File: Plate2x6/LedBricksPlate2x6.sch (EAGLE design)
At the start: 8 parts

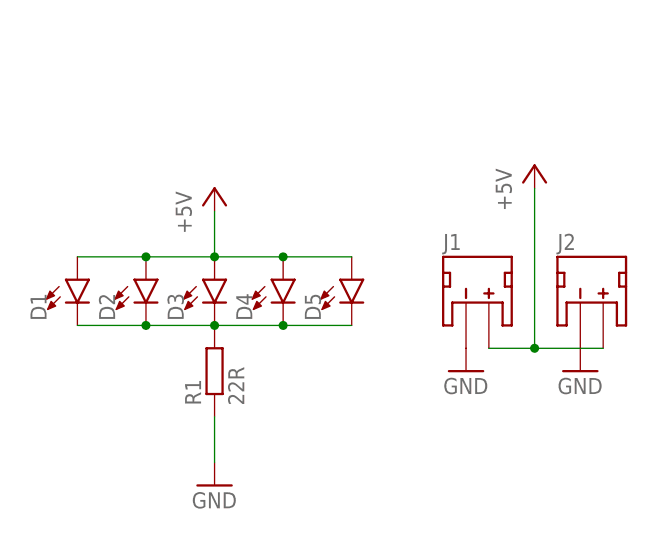
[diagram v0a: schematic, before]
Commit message: change connector to jst sh
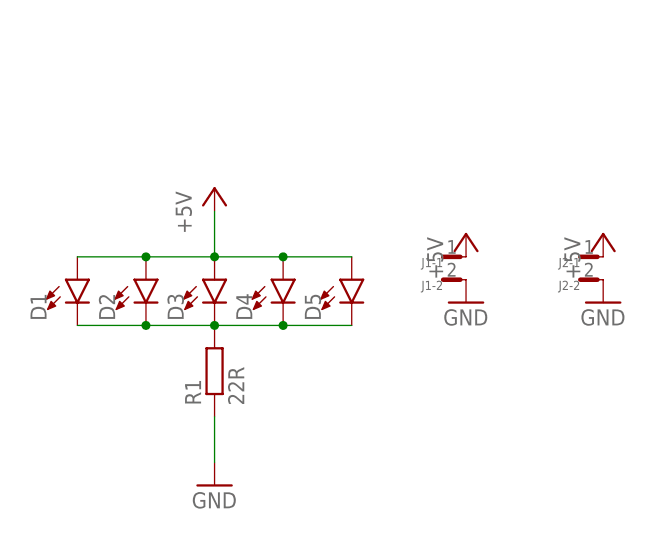
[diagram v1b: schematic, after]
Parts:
- J1, J2: value (none) -> SM02B-SRSS-TB; device SparkFun-Connectors:JST_2MM_MALE -> con-JST-SH:SM02B-SRSS-TB
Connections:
- net +5V: now also J1-1.P, J2-1.P; no longer J1.+, J2.+
- net GND: now also J1-2.P, J2-2.P; no longer J1.-, J2.-
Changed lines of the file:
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@@
 <part name="P+1" library="supply1" library_urn="urn:adsk.eagle:library:371" deviceset="+5V" device=""/>
 <part name="GND1" library="supply1" library_urn="urn:adsk.eagle:library:371" deviceset="GND" device=""/>
-<part name="J1" library="SparkFun-Connectors" library_urn="urn:adsk.eagle:library:513" deviceset="JST_2MM_MALE" device="" package3d_urn="urn:adsk.eagle:package:38042/1"/>
-<part name="J2" library="SparkFun-Connectors" library_urn="urn:adsk.eagle:library:513" deviceset="JST_2MM_MALE" device="" package3d_urn="urn:adsk.eagle:package:38042/1"/>
 <part name="GND2" library="supply1" library_urn="urn:adsk.eagle:library:371" deviceset="GND" device=""/>
 <part name="GND3" library="supply1" library_urn="urn:adsk.eagle:library:371" deviceset="GND" device=""/>
 <part name="P+2" library="supply1" library_urn="urn:adsk.eagle:library:371" deviceset="+5V" device=""/>
+<part name="J1" library="con-JST-SH" deviceset="SM02B-SRSS-TB" device=""/>
+<part name="J2" library="con-JST-SH" deviceset="SM02B-SRSS-TB" device=""/>
+<part name="P+3" library="supply1" library_urn="urn:adsk.eagle:library:371" deviceset="+5V" device=""/>
 </parts>
 <sheets>
@@
 <attribute name="VALUE" x="15.24" y="-25.4" size="1.778" layer="96"/>
 </instance>
-<instance part="J1" gate="G$1" x="45.72" y="-2.54" smashed="yes">
-<attribute name="NAME" x="43.18" y="3.302" size="1.778" layer="95"/>
+<instance part="GND2" gate="1" x="45.72" y="-2.54" smashed="yes">
+<attribute name="VALUE" x="43.18" y="-5.08" size="1.778" layer="96"/>
 </instance>
-<instance part="J2" gate="G$1" x="58.42" y="-2.54" smashed="yes">
-<attribute name="NAME" x="55.88" y="3.302" size="1.778" layer="95"/>
+<instance part="GND3" gate="1" x="60.96" y="-2.54" smashed="yes">
+<attribute name="VALUE" x="58.42" y="-5.08" size="1.778" layer="96"/>
 </instance>
-<instance part="GND2" gate="1" x="45.72" y="-10.16" smashed="yes">
-<attribute name="VALUE" x="43.18" y="-12.7" size="1.778" layer="96"/>
+<instance part="P+2" gate="1" x="45.72" y="5.08" smashed="yes">
+<attribute name="VALUE" x="43.18" y="0" size="1.778" layer="96" rot="R90"/>
 </instance>
-<instance part="GND3" gate="1" x="58.42" y="-10.16" smashed="yes">
-<attribute name="VALUE" x="55.88" y="-12.7" size="1.778" layer="96"/>
+<instance part="J1" gate="-1" x="43.18" y="2.54" smashed="yes">
+<attribute name="NAME" x="43.18" y="1.905" size="1.016" layer="95" rot="R180" align="center-left"/>
 </instance>
-<instance part="P+2" gate="1" x="53.34" y="12.7" smashed="yes">
-<attribute name="VALUE" x="50.8" y="7.62" size="1.778" layer="96" rot="R90"/>
+<instance part="J1" gate="-2" x="43.18" y="0" smashed="yes">
+<attribute name="NAME" x="43.18" y="-0.635" size="1.016" layer="95" rot="R180" align="center-left"/>
+</instance>
+<instance part="J2" gate="-1" x="58.42" y="2.54" smashed="yes">
+<attribute name="NAME" x="58.42" y="1.905" size="1.016" layer="95" rot="R180" align="center-left"/>
+</instance>
+<instance part="J2" gate="-2" x="58.42" y="0" smashed="yes">
+<attribute name="NAME" x="58.42" y="-0.635" size="1.016" layer="95" rot="R180" align="center-left"/>
+</instance>
+<instance part="P+3" gate="1" x="60.96" y="5.08" smashed="yes">
+<attribute name="VALUE" x="58.42" y="0" size="1.778" layer="96" rot="R90"/>
 </instance>
 </instances>
@@
 </segment>
 <segment>
-<pinref part="J1" gate="G$1" pin="+"/>
-<pinref part="J2" gate="G$1" pin="+"/>
-<wire x1="48.26" y1="-7.62" x2="53.34" y2="-7.62" width="0.1524" layer="91"/>
-<wire x1="53.34" y1="-7.62" x2="60.96" y2="-7.62" width="0.1524" layer="91"/>
-<wire x1="53.34" y1="-7.62" x2="53.34" y2="10.16" width="0.1524" layer="91"/>
-<junction x="53.34" y="-7.62"/>
+<pinref part="J1" gate="-1" pin="P"/>
 <pinref part="P+2" gate="1" pin="+5V"/>
+</segment>
+<segment>
+<pinref part="J2" gate="-1" pin="P"/>
+<pinref part="P+3" gate="1" pin="+5V"/>
 </segment>
 </net>
@@
 </segment>
 <segment>
-<pinref part="J1" gate="G$1" pin="-"/>
+<pinref part="J1" gate="-2" pin="P"/>
 <pinref part="GND2" gate="1" pin="GND"/>
 </segment>
 <segment>
-<pinref part="J2" gate="G$1" pin="-"/>
+<pinref part="J2" gate="-2" pin="P"/>
 <pinref part="GND3" gate="1" pin="GND"/>
 </segment>

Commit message: gerbers, pnp file
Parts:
- D1, D2, D3, D4, D5: value (none) -> XL-3216WWC
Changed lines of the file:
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@@
 </classes>
 <parts>
-<part name="D1" library="SparkFun-LED" library_urn="urn:adsk.eagle:library:529" deviceset="LED" device="1206" package3d_urn="urn:adsk.eagle:package:39352/1"/>
-<part name="D2" library="SparkFun-LED" library_urn="urn:adsk.eagle:library:529" deviceset="LED" device="1206" package3d_urn="urn:adsk.eagle:package:39352/1"/>
-<part name="D3" library="SparkFun-LED" library_urn="urn:adsk.eagle:library:529" deviceset="LED" device="1206" package3d_urn="urn:adsk.eagle:package:39352/1"/>
-<part name="D4" library="SparkFun-LED" library_urn="urn:adsk.eagle:library:529" deviceset="LED" device="1206" package3d_urn="urn:adsk.eagle:package:39352/1"/>
-<part name="D5" library="SparkFun-LED" library_urn="urn:adsk.eagle:library:529" deviceset="LED" device="1206" package3d_urn="urn:adsk.eagle:package:39352/1"/>
+<part name="D1" library="SparkFun-LED" library_urn="urn:adsk.eagle:library:529" deviceset="LED" device="1206" package3d_urn="urn:adsk.eagle:package:39352/1" value="XL-3216WWC"/>
+<part name="D2" library="SparkFun-LED" library_urn="urn:adsk.eagle:library:529" deviceset="LED" device="1206" package3d_urn="urn:adsk.eagle:package:39352/1" value="XL-3216WWC"/>
+<part name="D3" library="SparkFun-LED" library_urn="urn:adsk.eagle:library:529" deviceset="LED" device="1206" package3d_urn="urn:adsk.eagle:package:39352/1" value="XL-3216WWC"/>
+<part name="D4" library="SparkFun-LED" library_urn="urn:adsk.eagle:library:529" deviceset="LED" device="1206" package3d_urn="urn:adsk.eagle:package:39352/1" value="XL-3216WWC"/>
+<part name="D5" library="SparkFun-LED" library_urn="urn:adsk.eagle:library:529" deviceset="LED" device="1206" package3d_urn="urn:adsk.eagle:package:39352/1" value="XL-3216WWC"/>
 <part name="R1" library="resistor" library_urn="urn:adsk.eagle:library:348" deviceset="R-EU_" device="R0805" package3d_urn="urn:adsk.eagle:package:23553/2" value="22R"/>
 <part name="P+1" library="supply1" library_urn="urn:adsk.eagle:library:371" deviceset="+5V" device=""/>
@@
 <instances>
 <instance part="D1" gate="G$1" x="2.54" y="0" smashed="yes">
-<attribute name="NAME" x="-0.889" y="-4.572" size="1.778" layer="95" font="vector" rot="R90"/>
-<attribute name="VALUE" x="4.445" y="-4.572" size="1.778" layer="96" font="vector" rot="R90" align="top-left"/>
+<attribute name="NAME" x="3.556" y="-4.699" size="1.778" layer="95" font="vector"/>
+<attribute name="VALUE" x="-3.175" y="0.508" size="1.778" layer="96" font="vector" rot="R90" align="top-left"/>
 </instance>
 <instance part="D2" gate="G$1" x="10.16" y="0" smashed="yes">
-<attribute name="NAME" x="6.731" y="-4.572" size="1.778" layer="95" font="vector" rot="R90"/>
-<attribute name="VALUE" x="12.065" y="-4.572" size="1.778" layer="96" font="vector" rot="R90" align="top-left"/>
+<attribute name="NAME" x="11.176" y="-4.445" size="1.778" layer="95" font="vector"/>
+<attribute name="VALUE" x="4.445" y="0.508" size="1.778" layer="96" font="vector" rot="R90" align="top-left"/>
 </instance>
 <instance part="D3" gate="G$1" x="17.78" y="0" smashed="yes">
-<attribute name="NAME" x="14.351" y="-4.572" size="1.778" layer="95" font="vector" rot="R90"/>
-<attribute name="VALUE" x="19.685" y="-4.572" size="1.778" layer="96" font="vector" rot="R90" align="top-left"/>
+<attribute name="NAME" x="18.796" y="-4.445" size="1.778" layer="95" font="vector"/>
+<attribute name="VALUE" x="14.605" y="0.508" size="1.778" layer="96" font="vector" rot="R90" align="top-left"/>
 </instance>
 <instance part="D4" gate="G$1" x="25.4" y="0" smashed="yes">
-<attribute name="NAME" x="21.971" y="-4.572" size="1.778" layer="95" font="vector" rot="R90"/>
-<attribute name="VALUE" x="27.305" y="-4.572" size="1.778" layer="96" font="vector" rot="R90" align="top-left"/>
+<attribute name="NAME" x="26.67" y="-4.445" size="1.778" layer="95" font="vector"/>
+<attribute name="VALUE" x="24.511" y="3.81" size="1.778" layer="96" font="vector" rot="R90" align="top-left"/>
 </instance>
 <instance part="D5" gate="G$1" x="33.02" y="0" smashed="yes">
-<attribute name="NAME" x="29.591" y="-4.572" size="1.778" layer="95" font="vector" rot="R90"/>
-<attribute name="VALUE" x="34.925" y="-4.572" size="1.778" layer="96" font="vector" rot="R90" align="top-left"/>
+<attribute name="NAME" x="34.798" y="-5.715" size="1.778" layer="95" font="vector"/>
+<attribute name="VALUE" x="32.131" y="3.048" size="1.778" layer="96" font="vector" rot="R90" align="top-left"/>
 </instance>
 <instance part="R1" gate="G$1" x="17.78" y="-10.16" smashed="yes" rot="R90">
-<attribute name="NAME" x="16.2814" y="-13.97" size="1.778" layer="95" rot="R90"/>
-<attribute name="VALUE" x="21.082" y="-13.97" size="1.778" layer="96" rot="R90"/>
+<attribute name="NAME" x="20.066" y="-11.4554" size="1.778" layer="95"/>
+<attribute name="VALUE" x="20.066" y="-14.224" size="1.778" layer="96"/>
 </instance>
-<instance part="P+1" gate="1" x="17.78" y="10.16" smashed="yes">
-<attribute name="VALUE" x="15.24" y="5.08" size="1.778" layer="96" rot="R90"/>
+<instance part="P+1" gate="1" x="17.78" y="25.4" smashed="yes">
+<attribute name="VALUE" x="15.748" y="26.416" size="1.778" layer="96"/>
 </instance>
 <instance part="GND1" gate="1" x="17.78" y="-22.86" smashed="yes">
@@
 <attribute name="VALUE" x="58.42" y="-5.08" size="1.778" layer="96"/>
 </instance>
-<instance part="P+2" gate="1" x="45.72" y="5.08" smashed="yes">
-<attribute name="VALUE" x="43.18" y="0" size="1.778" layer="96" rot="R90"/>
+<instance part="P+2" gate="1" x="45.72" y="10.16" smashed="yes">
+<attribute name="VALUE" x="43.688" y="11.176" size="1.778" layer="96"/>
 </instance>
 <instance part="J1" gate="-1" x="43.18" y="2.54" smashed="yes">
@@
 <attribute name="NAME" x="58.42" y="-0.635" size="1.016" layer="95" rot="R180" align="center-left"/>
 </instance>
-<instance part="P+3" gate="1" x="60.96" y="5.08" smashed="yes">
-<attribute name="VALUE" x="58.42" y="0" size="1.778" layer="96" rot="R90"/>
+<instance part="P+3" gate="1" x="60.96" y="10.16" smashed="yes">
+<attribute name="VALUE" x="58.928" y="11.176" size="1.778" layer="96"/>
 </instance>
 </instances>
@@
 <wire x1="25.4" y1="2.54" x2="33.02" y2="2.54" width="0.1524" layer="91"/>
 <junction x="25.4" y="2.54"/>
-<wire x1="17.78" y1="2.54" x2="17.78" y2="7.62" width="0.1524" layer="91"/>
+<wire x1="17.78" y1="2.54" x2="17.78" y2="22.86" width="0.1524" layer="91"/>
 <pinref part="P+1" gate="1" pin="+5V"/>
 </segment>
@@
 <pinref part="J1" gate="-1" pin="P"/>
 <pinref part="P+2" gate="1" pin="+5V"/>
+<wire x1="45.72" y1="7.62" x2="45.72" y2="2.54" width="0.1524" layer="91"/>
 </segment>
 <segment>
 <pinref part="J2" gate="-1" pin="P"/>
 <pinref part="P+3" gate="1" pin="+5V"/>
+<wire x1="60.96" y1="7.62" x2="60.96" y2="2.54" width="0.1524" layer="91"/>
 </segment>
 </net>
